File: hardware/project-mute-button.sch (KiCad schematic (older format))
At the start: 6 parts, among them J1 Conn_01x06_Female, J2 Conn_01x06_Female, J3 Button, J4 Toggle Switch

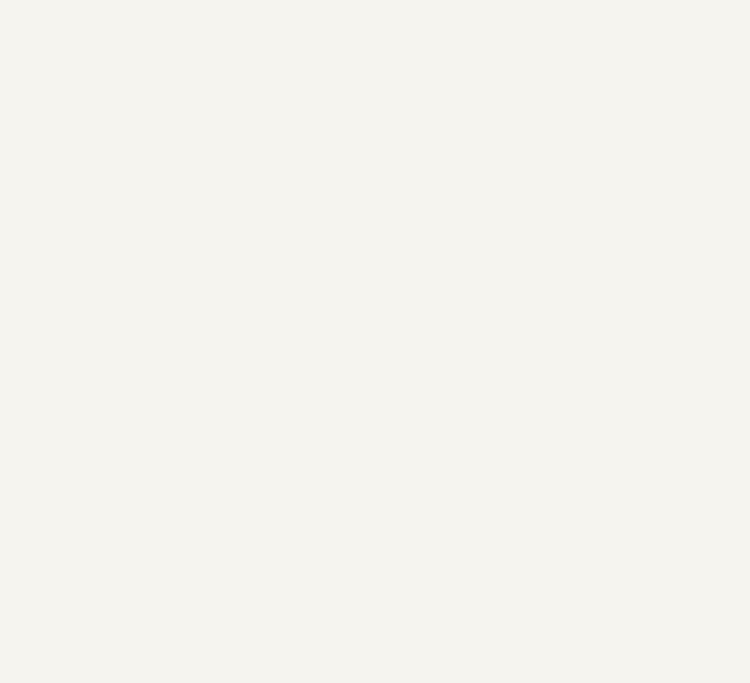
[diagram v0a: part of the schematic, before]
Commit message: Add 2 leds to schematic
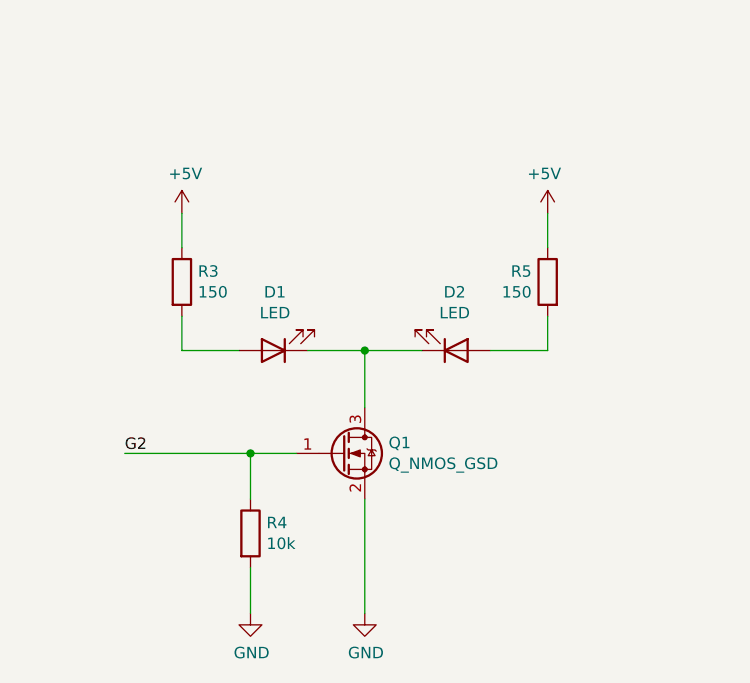
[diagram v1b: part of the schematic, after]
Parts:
- added D1, D2: LED, LED_SMD:LED_0603_1608Metric, symbol Device:LED
- added Q1: Q_NMOS_GSD, Package_TO_SOT_SMD:SOT-323_SC-70, symbol Device:Q_NMOS_GSD
- added R3, R5: 150, Resistor_SMD:R_0603_1608Metric, symbol Device:R
- added R4: 10k, Resistor_SMD:R_0603_1608Metric, symbol Device:R
- R1, R2: footprint (none) -> Resistor_SMD:R_0603_1608Metric
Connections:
- net +5V: now also R3.1, R5.1
- net G2: now also Q1.1 (G), R4.1
- net GND: now also Q1.2 (S), R4.2
- new net: D1.1 (K), D2.1 (K), Q1.3 (D)
- new net: D1.2 (A), R3.2
- new net: D2.2 (A), R5.2
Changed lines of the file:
@@
 F 0 "R1" H 4120 1296 50  0000 L CNN
 F 1 "10k" H 4120 1205 50  0000 L CNN
-F 2 "" V 3980 1250 50  0001 C CNN
+F 2 "Resistor_SMD:R_0603_1608Metric" V 3980 1250 50  0001 C CNN
 F 3 "~" H 4050 1250 50  0001 C CNN
 	1    4050 1250
@@
 F 0 "R2" H 5770 1246 50  0000 L CNN
 F 1 "10k" H 5770 1155 50  0000 L CNN
-F 2 "" V 5630 1200 50  0001 C CNN
+F 2 "Resistor_SMD:R_0603_1608Metric" V 5630 1200 50  0001 C CNN
 F 3 "~" H 5700 1200 50  0001 C CNN
 	1    5700 1200
@@
 	1    0    0    -1
 $EndComp
+$Comp
+L Device:LED D1
+U 1 1 636705E7
+P 1850 3300
+F 0 "D1" H 1843 3045 50  0000 C CNN
+F 1 "LED" H 1843 3136 50  0000 C CNN
+F 2 "LED_SMD:LED_0603_1608Metric" H 1850 3300 50  0001 C CNN
+F 3 "~" H 1850 3300 50  0001 C CNN
+	1    1850 3300
+	-1   0    0    1
+$EndComp
+$Comp
+L Device:R R3
+U 1 1 6367154E
+P 1450 3000
+F 0 "R3" H 1520 3046 50  0000 L CNN
+F 1 "150" H 1520 2955 50  0000 L CNN
+F 2 "Resistor_SMD:R_0603_1608Metric" V 1380 3000 50  0001 C CNN
+F 3 "~" H 1450 3000 50  0001 C CNN
+	1    1450 3000
+	1    0    0    -1
+$EndComp
+$Comp
+L Device:R R4
+U 1 1 63675FFE
+P 1750 4100
+F 0 "R4" H 1820 4146 50  0000 L CNN
+F 1 "10k" H 1820 4055 50  0000 L CNN
+F 2 "Resistor_SMD:R_0603_1608Metric" V 1680 4100 50  0001 C CNN
+F 3 "~" H 1750 4100 50  0001 C CNN
+	1    1750 4100
+	1    0    0    -1
+$EndComp
+$Comp
+L power:GND #PWR09
+U 1 1 63676482
+P 2250 4450
+F 0 "#PWR09" H 2250 4200 50  0001 C CNN
+F 1 "GND" H 2255 4277 50  0000 C CNN
+F 2 "" H 2250 4450 50  0001 C CNN
+F 3 "" H 2250 4450 50  0001 C CNN
+	1    2250 4450
+	1    0    0    -1
+$EndComp
+$Comp
+L power:GND #PWR08
+U 1 1 63676A5C
+P 1750 4450
+F 0 "#PWR08" H 1750 4200 50  0001 C CNN
+F 1 "GND" H 1755 4277 50  0000 C CNN
+F 2 "" H 1750 4450 50  0001 C CNN
+F 3 "" H 1750 4450 50  0001 C CNN
+	1    1750 4450
+	1    0    0    -1
+$EndComp
+$Comp
+L power:+5V #PWR07
+U 1 1 63676E1F
+P 1450 2700
+F 0 "#PWR07" H 1450 2550 50  0001 C CNN
+F 1 "+5V" H 1465 2873 50  0000 C CNN
+F 2 "" H 1450 2700 50  0001 C CNN
+F 3 "" H 1450 2700 50  0001 C CNN
+	1    1450 2700
+	1    0    0    -1
+$EndComp
+Wire Wire Line
+	1450 2700 1450 2850
+Wire Wire Line
+	1450 3150 1450 3300
+Wire Wire Line
+	1450 3300 1700 3300
+Wire Wire Line
+	2000 3300 2250 3300
+Wire Wire Line
+	2250 3300 2250 3550
+Text Label 1200 3750 0    50   ~ 0
+G2
+Wire Wire Line
+	1200 3750 1750 3750
+Wire Wire Line
+	1750 3950 1750 3750
+Connection ~ 1750 3750
+Wire Wire Line
+	1750 3750 1950 3750
+Wire Wire Line
+	1750 4250 1750 4450
+Wire Wire Line
+	2250 3950 2250 4450
+$Comp
+L Device:LED D2
+U 1 1 63681E8C
+P 2650 3300
+F 0 "D2" H 2643 3045 50  0000 C CNN
+F 1 "LED" H 2643 3136 50  0000 C CNN
+F 2 "LED_SMD:LED_0603_1608Metric" H 2650 3300 50  0001 C CNN
+F 3 "~" H 2650 3300 50  0001 C CNN
+	1    2650 3300
+	1    0    0    1
+$EndComp
+$Comp
+L Device:R R5
+U 1 1 63681E92
+P 3050 3000
+F 0 "R5" H 3120 3046 50  0000 L CNN
+F 1 "150" H 3120 2955 50  0000 L CNN
+F 2 "Resistor_SMD:R_0603_1608Metric" V 2980 3000 50  0001 C CNN
+F 3 "~" H 3050 3000 50  0001 C CNN
+	1    3050 3000
+	-1   0    0    -1
+$EndComp
+$Comp
+L power:+5V #PWR010
+U 1 1 63681E98
+P 3050 2700
+F 0 "#PWR010" H 3050 2550 50  0001 C CNN
+F 1 "+5V" H 3065 2873 50  0000 C CNN
+F 2 "" H 3050 2700 50  0001 C CNN
+F 3 "" H 3050 2700 50  0001 C CNN
+	1    3050 2700
+	-1   0    0    -1
+$EndComp
+Wire Wire Line
+	3050 2700 3050 2850
+Wire Wire Line
+	3050 3150 3050 3300
+Wire Wire Line
+	3050 3300 2800 3300
+Wire Wire Line
+	2500 3300 2250 3300
+Connection ~ 2250 3300
+$Comp
+L Device:Q_NMOS_GSD Q1
+U 1 1 63674C1F
+P 2150 3750
+F 0 "Q1" H 2354 3796 50  0000 L CNN
+F 1 "Q_NMOS_GSD" H 2354 3705 50  0000 L CNN
+F 2 "Package_TO_SOT_SMD:SOT-323_SC-70" H 2350 3850 50  0001 C CNN
+F 3 "~" H 2150 3750 50  0001 C CNN
+	1    2150 3750
+	1    0    0    -1
+$EndComp

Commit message: First placement with board shape
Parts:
- added H1, H2, H3, H4: MountingHole, MountingHole:MountingHole_5mm, symbol Mechanical:MountingHole
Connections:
- no-connect marks 0 -> 6
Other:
- note added: "PCB to case"
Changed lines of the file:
@@
 	1    0    0    -1
 $EndComp
+$Comp
+L Mechanical:MountingHole H1
+U 1 1 636A1891
+P 4500 2750
+F 0 "H1" H 4600 2750 50  0000 L CNN
+F 1 "MountingHole" H 4600 2705 50  0001 L CNN
+F 2 "MountingHole:MountingHole_5mm" H 4500 2750 50  0001 C CNN
+F 3 "~" H 4500 2750 50  0001 C CNN
+	1    4500 2750
+	1    0    0    -1
+$EndComp
+$Comp
+L Mechanical:MountingHole H3
+U 1 1 636A2ED1
+P 4850 2750
+F 0 "H3" H 4950 2750 50  0000 L CNN
+F 1 "MountingHole" H 4950 2705 50  0001 L CNN
+F 2 "MountingHole:MountingHole_5mm" H 4850 2750 50  0001 C CNN
+F 3 "~" H 4850 2750 50  0001 C CNN
+	1    4850 2750
+	1    0    0    -1
+$EndComp
+$Comp
+L Mechanical:MountingHole H2
+U 1 1 636A635D
+P 4500 2950
+F 0 "H2" H 4600 2950 50  0000 L CNN
+F 1 "MountingHole" H 4600 2905 50  0001 L CNN
+F 2 "MountingHole:MountingHole_5mm" H 4500 2950 50  0001 C CNN
+F 3 "~" H 4500 2950 50  0001 C CNN
+	1    4500 2950
+	1    0    0    -1
+$EndComp
+$Comp
+L Mechanical:MountingHole H4
+U 1 1 636A6363
+P 4850 2950
+F 0 "H4" H 4950 2950 50  0000 L CNN
+F 1 "MountingHole" H 4950 2905 50  0001 L CNN
+F 2 "MountingHole:MountingHole_5mm" H 4850 2950 50  0001 C CNN
+F 3 "~" H 4850 2950 50  0001 C CNN
+	1    4850 2950
+	1    0    0    -1
+$EndComp
+Text Notes 4450 2600 0    50   ~ 0
+PCB to case
+NoConn ~ 1300 1400
+NoConn ~ 1300 1500
+NoConn ~ 1300 1600
+NoConn ~ 2200 1100
+NoConn ~ 2200 1200
+NoConn ~ 2200 1300
 $EndSCHEMATC
